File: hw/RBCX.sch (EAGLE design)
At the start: 473 parts, among them IC1 AMS1117-3.3, IC10 INA180A4, IC11 INA180A4, IC12 MPU-6050, IC13 STM32F103VCT6, IC2 DRV8833PWP, IC3 INA180A4, IC4 INA180A4, IC5 DRV8833PWP, IC6 INA180A4, IC7 INA180A4, IC8 INA180A4, IC9 INA180A4, P1 M1, P2 M2, P3 M3, P4 M4, Q1 NCE20P45Q, Q10 2N7002, Q2 NCE20P45Q, Q3 2N7002, Q4 2N7002, Q5 2N7002, Q6 2N7002, Q7 2N7002, Q8 2N7002, Q9 2N7002, X1 POWER_IN, X2 POWER_OUT, X3 52559-3092, X4 uUSB, Y1 5032/2P, Y2 3215_2P

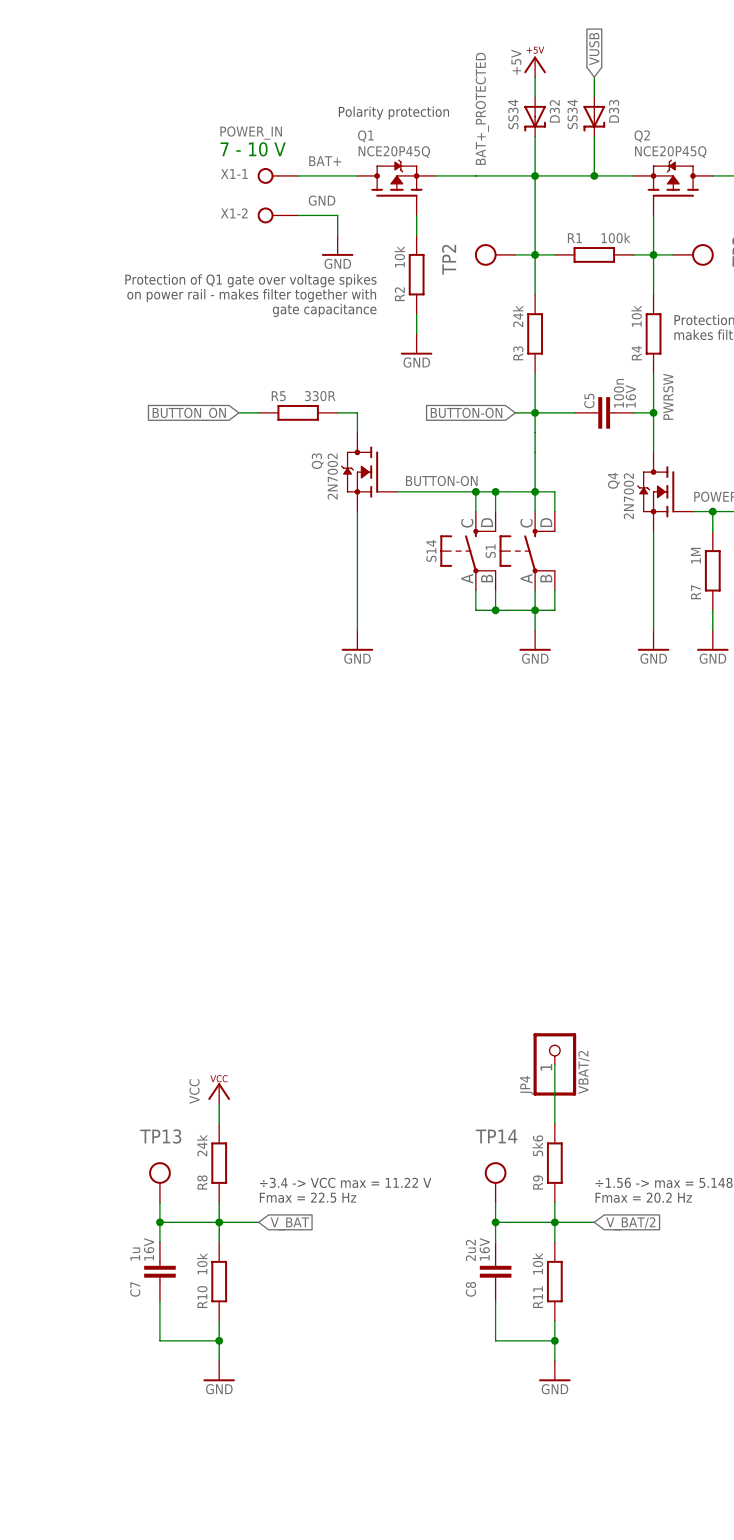
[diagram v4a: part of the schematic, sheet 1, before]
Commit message: hw: add middle battery voltage (with overvoltage protection) to the power input terminal block (replaced by 3-pin)
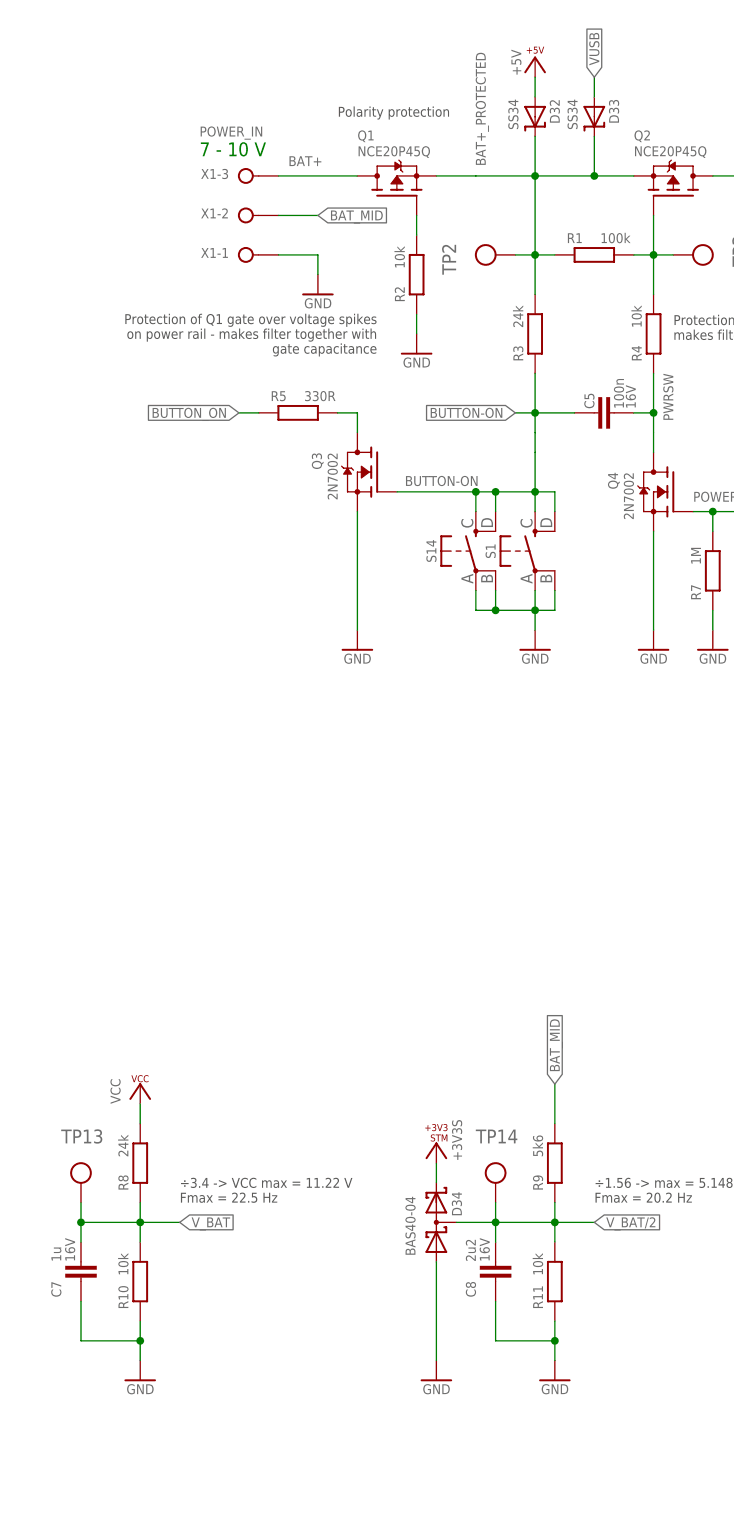
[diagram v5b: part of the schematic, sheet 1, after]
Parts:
- removed JP4: VBAT/2, pinhead:PINHD-1X1
- added D34: BAS40-04, diode:BAS40-04
- X1: device con-wago-508:W237-02P -> con-wago-508:W237-03P
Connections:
- removed net VBAT/2: JP4.1, R9.2
- new net BAT_MID: R9.2, X1-2.KL
- net +3V3S: now also D34.C2
- net BAT+: now also X1-3.KL; no longer X1-1.KL
- net GND: now also D34.A1, X1-1.KL; no longer X1-2.KL
- net V_BAT/2: now also D34.C1A2
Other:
- moved on the sheet: C7, R10, R8, TP13, X1-1, X1-2
